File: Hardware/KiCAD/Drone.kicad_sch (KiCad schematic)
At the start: 15 parts

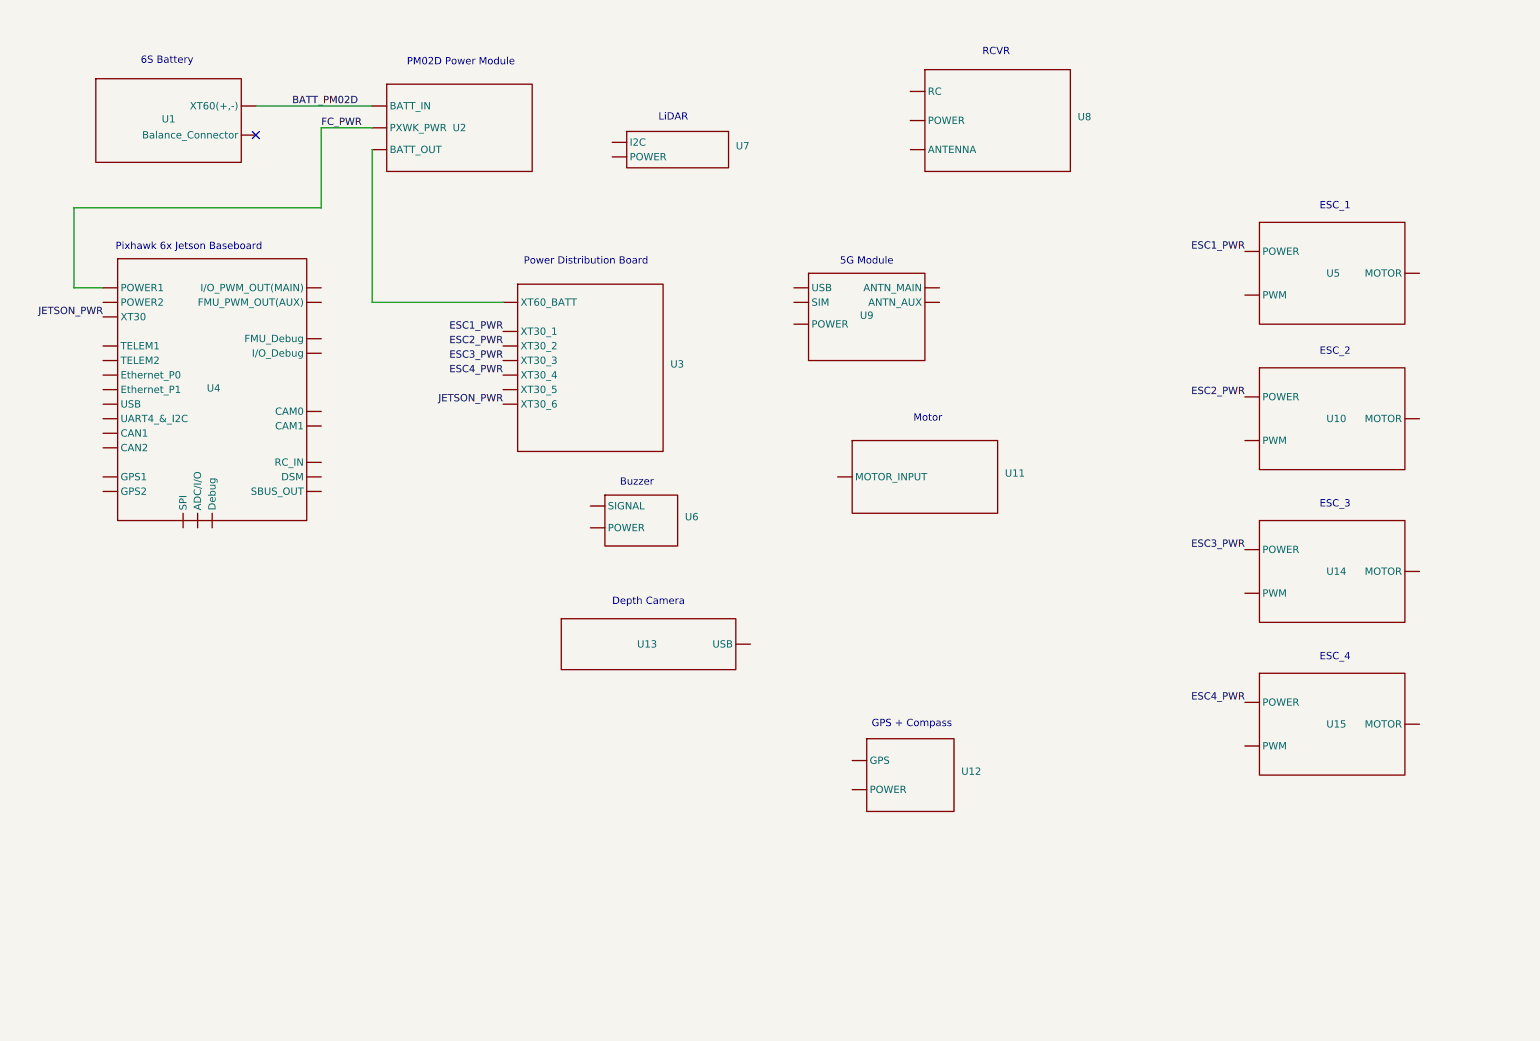
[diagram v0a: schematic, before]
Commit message: Created General Schematics V1, updated componens accordingly
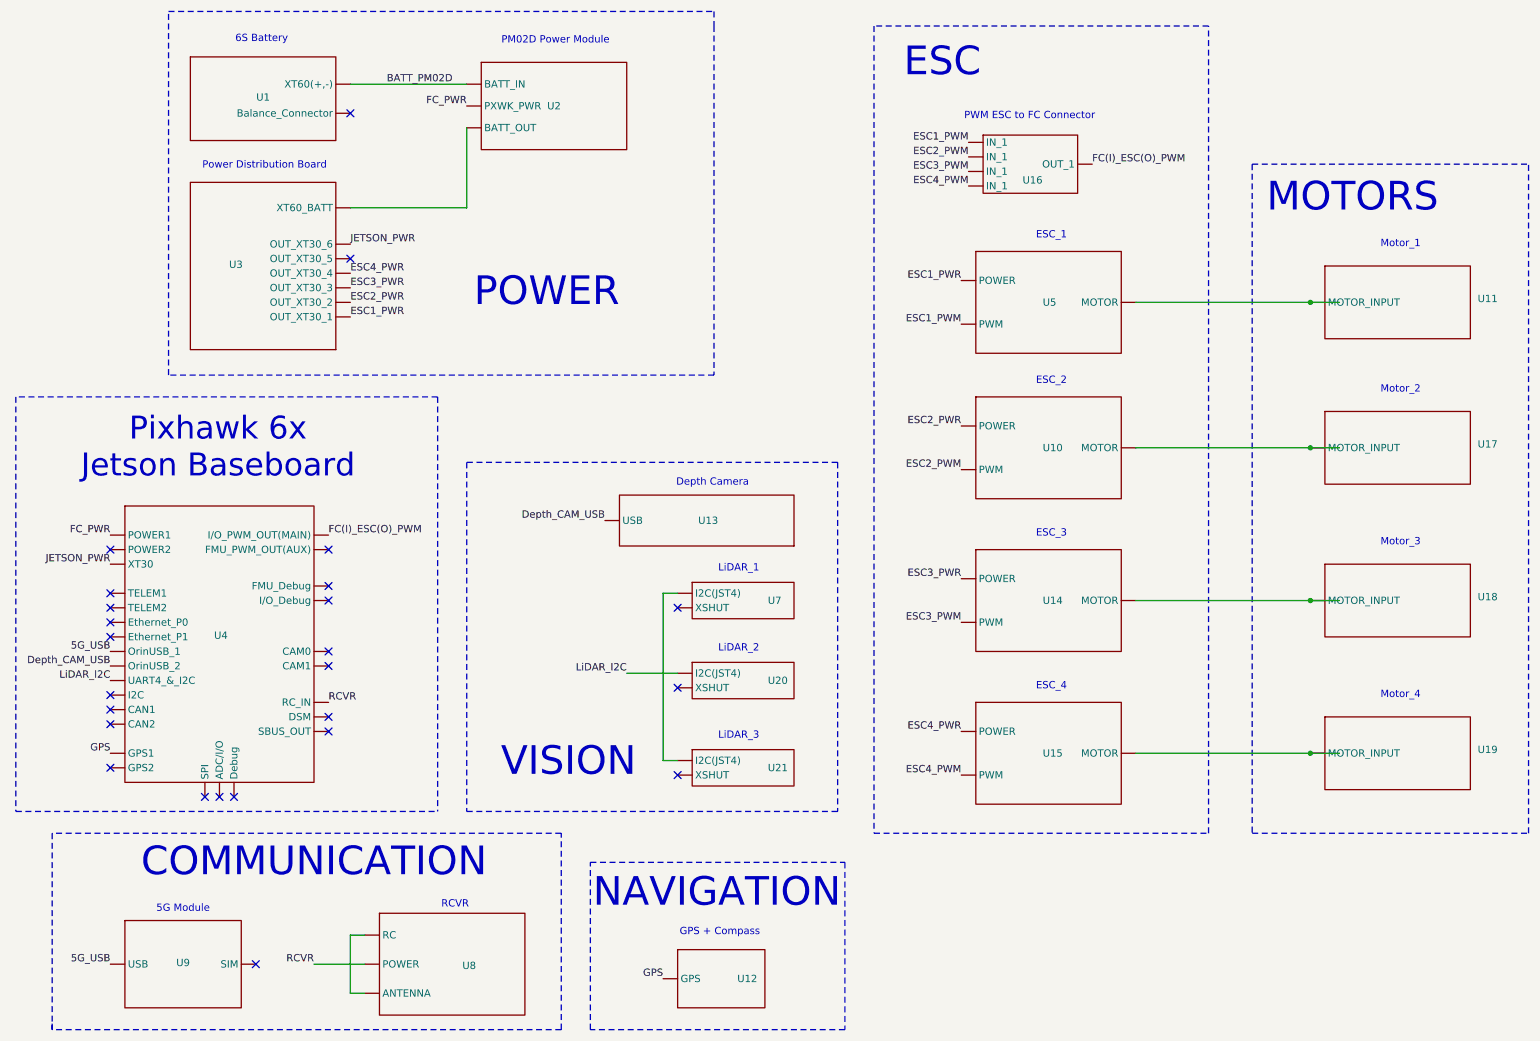
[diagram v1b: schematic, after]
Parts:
- removed U6: ~, symbol Drone_SYMBOLS:VIFLY_Finder_V2
- added U16: ~, symbol Drone_SYMBOLS:Conn_04to01
- added U17, U18, U19: ~, symbol Drone_SYMBOLS:MN2806_EVO_KV650
- added U20, U21: ~, symbol Drone_SYMBOLS:ST_VL53L1X_Lidar
- U12: symbol Drone_SYMBOLS:Micro_M10_GPS -> Drone_SYMBOLS:M10_GPS
- U9: symbol Drone_SYMBOLS:Quectel_RM520N-GL_5G -> Drone_SYMBOLS:D-Link_D501_5G_USB_Adapter
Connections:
- net RCVR: now reaches U8. (ANTENNA)
- net RCVR: now also U4. (SBUS_OUT)
- net at U7. (XSHUT): now also U21. (XSHUT)
- net at U11. (MOTOR_INPUT): now also U5. (MOTOR)
- net 5G_USB: now reaches U9. (SIM)
- net 5G_USB: now also U4. (SBUS_OUT)
- net GPS: now reaches U12. (GPS)
- net GPS: now also U4. (SBUS_OUT)
- net Depth_CAM_USB: now reaches U13. (USB)
- net Depth_CAM_USB: now also U4. (SBUS_OUT)
- new net: U2. (BATT_OUT), U3. (XT60_BATT)
- new net: U10. (MOTOR), U17. (MOTOR_INPUT)
- new net: U14. (MOTOR), U18. (MOTOR_INPUT)
- new net: U15. (MOTOR), U19. (MOTOR_INPUT)
- new net ESC1_PWM: U16. (OUT_1), U5. (MOTOR)
- new net ESC2_PWM: U10. (MOTOR), U16. (OUT_1)
- new net ESC3_PWM: U14. (MOTOR), U16. (OUT_1)
- new net ESC4_PWM: U15. (MOTOR), U16. (OUT_1)
- new net FC(I)_ESC(O)_PWM: U16. (OUT_1), U4. (SBUS_OUT)
- new net LiDAR_I2C: U20. (XSHUT), U4. (SBUS_OUT)
- no-connect marks 1 -> 25
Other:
- note added: "COMMUNICATION"
- note added: "ESC"
- note added: "LiDAR_1"
- note added: "LiDAR_2"
- note added: "LiDAR_3"
- note added: "MOTORS"
- note added: "Motor_1"
- note added: "Motor_2"
- note added: "Motor_3"
- note added: "Motor_4"
- note added: "NAVIGATION"
- note added: "POWER"
- note added: "PWM ESC to FC Connector"
- note added: "VISION"
- note removed: "Buzzer"
- note removed: "LiDAR"
- note removed: "Motor"
- title: (none) -> Drone General Schematics
- moved on the sheet: U1, U10, U11, U13, U14, U15, U2, U3, U5, U7, U8

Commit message: Added calculations for motor, props and ESC selection
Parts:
- added U6: ~, symbol Drone_SYMBOLS:Holybro_UBEC_12A
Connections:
- net JETSON_PWR: now also U6. (OUTPUT(XT30)); no longer U3. (XT60_BATT)
- net at U7. (XSHUT): now also U21. (XSHUT)
- net at U21. (XSHUT): no longer U7. (XSHUT)
- new net: U2. (BATT_OUT), U3. (XT60_BATT)
- new net: U3. (XT60_BATT), U6. (OUTPUT(XT30))
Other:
- note added: "UBEC"
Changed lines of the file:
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@@
+		)
+	)
+	(text "UBEC\n"
+		(exclude_from_sim no)
+		(at 106.934 68.58 0)
+		(effects
+			(font
+				(size 1.27 1.27)
+			)
 		)
 	)
@@
 	(text "POWER"
 		(exclude_from_sim no)
-		(at 107.95 64.262 0)
+		(at 115.062 46.99 0)
 		(effects
 			(font
@@
 		)
 	)
+	(wire
+		(pts
+			(xy 73.66 55.88) (xy 93.98 55.88)
+		)
+		(stroke
+			(width 0)
+			(type default)
+		)
+	)
 	(polyline
 		(pts
@@
 		)
 	)
-	(label "JETSON_PWR"
-		(at 73.66 55.88 0)
-		(effects
-			(font
-				(size 1.27 1.27)
-			)
-			(justify left bottom)
-		)
-	)
 	(label "5G_USB"
 		(at 31.75 127 180)
@@
 			)
 			(justify right bottom)
+		)
+	)
+	(label "JETSON_PWR"
+		(at 119.38 63.5 0)
+		(effects
+			(font
+				(size 1.27 1.27)
+			)
+			(justify left bottom)
 		)
 	)
@@
 					(unit 1)
 				)
+			)
+		)
+	)
+	(symbol
+		(lib_id "Drone_SYMBOLS:Holybro_UBEC_12A")
+		(at 106.68 59.69 0)
+		(unit 1)
+		(exclude_from_sim no)
+		(in_bom yes)
+		(on_board yes)
+		(dnp no)
+		(property "Reference" "U6"
+			(at 106.68 59.69 0)
+			(effects
+				(font
+					(size 1.27 1.27)
+				)
+			)
+		)
+		(property "Value" "~"
+			(at 106.68 52.07 0)
+			(effects
+				(font
+					(size 1.27 1.27)
+				)
+			)
+		)
+		(property "Footprint" ""
+			(at 106.68 59.69 0)
+			(effects
+				(font
+					(size 1.27 1.27)
+				)
+				(hide yes)
+			)
+		)
+		(property "Datasheet" ""
+			(at 106.68 59.69 0)
+			(effects
+				(font
+					(size 1.27 1.27)
+				)
+				(hide yes)
+			)
+		)
+		(property "Description" ""
+			(at 106.68 59.69 0)
+			(effects
+				(font
+					(size 1.27 1.27)
+				)
+				(hide yes)
+			)
+		)
+		(pin ""
+		)
+		(pin ""
+		)
+		(instances
+			(project ""
+				(path "/dbeab996-a2b6-48e4-a4c7-f60c74c79e5e"
+					(reference "U6")
+					(unit 1)
+				)

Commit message: Added plates
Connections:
- net at U7. (XSHUT): now also U21. (XSHUT)
- net at U21. (XSHUT): no longer U7. (XSHUT)
- new net: U2. (BATT_OUT), U3. (XT60_BATT)
- new net: U3. (XT60_BATT), U6. (OUTPUT(XT30))
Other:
- note added: "PWM EXT Board"
- note removed: "PWM ESC to FC Connector"
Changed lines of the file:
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@@
 		)
 	)
-	(text "PWM ESC to FC Connector"
+	(text "PWM EXT Board"
 		(exclude_from_sim no)
-		(at 192.278 33.528 0)
+		(at 192.786 35.306 0)
 		(effects
 			(font
